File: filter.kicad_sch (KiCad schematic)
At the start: 39 parts

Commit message: Update
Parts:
- removed C12, C14, C15, C17: C,IEC, symbol PCM_Generic-50:C,IEC
- removed C13, C16: C,IEC, symbol PCM_Generic:C,IEC
- removed R16, R17, R18, R20, R21, R22: R,IEC, symbol PCM_Generic:R,IEC
- added C18, C20: C,IEC, symbol PCM_Generic-50:C,IEC
- added C19: C,IEC, symbol PCM_Generic:C,IEC
- added R23, R24: R,IEC, symbol PCM_Generic:R,IEC
- R19: value R,IEC -> R HF ,IEC; Indicator + -> (none)
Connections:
- net GROUND: now also R15.1 (+); no longer C10.1 (+), C11.1 (+), R13.1 (+)
- net at C7.1 (+), R5.1 (+): now also C10.2 (-); no longer R8.1 (+)
- net at C6.2 (-), R6.1 (+): now also C1.2 (-), R1.1 (+), R13.2 (-); no longer R8.2 (-)
- net at C5.1 (+), R11.1 (+): no longer C10.2 (-)
- net at C11.2 (-): now also C2.1 (+), R2.1 (+)
- net at R9.1 (+): now also C19.1 (+), R23.2 (-); no longer R13.2 (-)
- net at C9.2 (-), R12.1 (+): now also R8.2 (-), C19.2 (-), R24.1 (+); no longer R9.2 (-)
- net at R15.2 (-): now also R8.1 (+)
- new net: C18.1 (+), C20.2 (-), R24.2 (-)
- new net: C18.2 (-), R9.2 (-)
- new net: C10.1 (+), C11.1 (+), R7.1 (+)
- new net: R13.1 (+), R19.2 (-), R7.2 (-)
- new net: C20.1 (+), R23.1 (+)
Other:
- note added: "Update 30/04/2023"
- moved on the sheet: C1, C10, C11, C2, C3, C4, C5, C6, C7, C8, C9, R1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

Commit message: Upgrade
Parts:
- removed C10, C11, C19: C,IEC, symbol PCM_Generic:C,IEC
- removed C18, C4, C5: C,IEC, symbol PCM_Generic-50:C,IEC
- added C10, C11, C12, C13, C19, C21, C22: C,IEC, symbol PCM_Generic-50:C,IEC
- added C14, C15, C16, C17, C18, C23, C24, C4, C5: C,IEC, symbol PCM_Generic:C,IEC
- added R16, R17, R18, R20, R21, R22, R25, R26, R27, R28, R29, R30, R31, R32: R,IEC, symbol PCM_Generic:R,IEC
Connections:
- net at C2.2 (-), R1.2 (-): now also C4.1 (+); no longer C3.1 (+)
- net at R11.1 (+): now also C9.1 (+), R12.2 (-)
- net at R5.1 (+): now also C1.2 (-), C6.2 (-), C9.2 (-), R10.1 (+), R13.1 (+), R19.1 (+), R3.1 (+), C16.2 (-), C17.2 (-), C18.2 (-), R17.1 (+), R18.1 (+), R20.1 (+), R21.1 (+), R26.1 (+); no longer C7.1 (+)
- net at R24.2 (-): now also C15.2 (-), C19.2 (-); no longer C20.2 (-)
- net at R9.2 (-): now also C6.1 (+), R8.1 (+)
- net at R7.1 (+): now also C8.1 (+), R9.1 (+)
- net at C2.1 (+): now also C3.2 (-), R3.2 (-); no longer R2.1 (+)
- net at R10.2 (-): now also C7.1 (+), C8.2 (-)
- net at R15.2 (-): now also R23.2 (-), R18.2 (-), R22.2 (-), R28.2 (-); no longer R8.1 (+)
- net at R14.1 (+): now also C16.1 (+), R27.2 (-)
- net at R14.2 (-): now also C12.2 (-), C23.1 (+)
- net at R4.2 (-): now also R5.2 (-), R6.2 (-), R7.2 (-); no longer C8.2 (-)
- net at C20.1 (+), R23.1 (+): now also R25.1 (+)
- net at C1.1 (+), R2.2 (-): now also R1.1 (+); no longer R3.1 (+)
- net GROUND: no longer names the net of R15.1 (+)
- net GROUND: now also R12.1 (+), C11.1 (+)
- new net: C18.1 (+), R24.1 (+), R25.2 (-)
- new net: C23.2 (-), C24.1 (+), R32.1 (+)
- new net: C4.2 (-), C5.1 (+), R6.1 (+)
- new net: C19.1 (+), C20.2 (-), R26.2 (-)
- new net: R17.2 (-), R19.2 (-), R30.2 (-), R31.2 (-), R32.2 (-)
- new net: C12.1 (+), C21.2 (-), R20.2 (-)
- new net: C5.2 (-), C7.2 (-), R8.2 (-)
- new net: C21.1 (+), R27.1 (+), R30.1 (+)
- new net: C10.2 (-), C14.1 (+), R11.2 (-)
- new net: C14.2 (-), C15.1 (+), R22.1 (+)
- new net: C3.1 (+), R2.1 (+), R4.1 (+)
- new net: C10.1 (+), C11.2 (-), R13.2 (-)
- new net: C13.1 (+), C22.2 (-), R21.2 (-)
- new net: C22.1 (+), R29.1 (+), R31.1 (+)
- new net: C17.1 (+), R16.1 (+), R29.2 (-)
- new net: C13.2 (-), C24.2 (-), R16.2 (-)
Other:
- note removed: "LINE"
- note removed: "MC 1230"
- note removed: "NEUTRAL"
- moved on the sheet: R19

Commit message: Upgrade
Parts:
- added R33, R34: R,IEC, symbol PCM_Generic:R,IEC
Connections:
- net at C15.2 (-), C19.2 (-), R24.2 (-): now also R34.1 (+)
- net at R15.2 (-), R18.2 (-), R22.2 (-)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: now also R34.2 (-)
- net at C10.2 (-), C14.1 (+), R11.2 (-): now also R33.1 (+)
- net at C11.1 (+), R12.1 (+), R15.1 (+): now also R33.2 (-)
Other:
- note added: "12"
- note added: "In real life"
- note added: "MC 1230"
- note added: "Update 17/07/2023"
- note removed: "1"
- note removed: "Update 30/04/2023"
- moved on the sheet: R17

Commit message: Upgrade
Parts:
- removed R15, R23, R7: R,IEC, symbol PCM_Generic:R,IEC
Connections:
- net at C23.2 (-), C24.1 (+), R32.1 (+): now also R17.2 (-), R19.2 (-), R30.2 (-), R32.2 (-)
- net at C1.2 (-), C16.2 (-), C17.2 (-)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: now also R30.1 (+), R31.1 (+), R4.1 (+)
- net at R18.2 (-), R22.2 (-), R28.2 (-)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: now also R4.2 (-)
- net at C21.1 (+), R27.1 (+): no longer R30.1 (+)
- net at R5.2 (-), R6.2 (-): now also R31.2 (-); no longer R4.2 (-)
- net at C3.1 (+), R2.1 (+): no longer R4.1 (+)
- net at C22.1 (+), R29.1 (+): no longer R31.1 (+)
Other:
- moved on the sheet: R17, R30, R31, R4

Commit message: Upgrade
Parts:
- added C25, C26: C,IEC, symbol PCM_Generic:C,IEC
- added R15, R23, R35, R7: R,IEC, symbol PCM_Generic:R,IEC
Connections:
- net at C1.2 (-), C16.2 (-), C17.2 (-)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: now also R28.1 (+), C25.2 (-), C26.1 (+), R15.1 (+), R23.2 (-), R35.2 (-)
- net at R18.2 (-), R22.2 (-), R28.2 (-)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: now also C14.2 (-), C15.1 (+), R22.1 (+), R23.1 (+)
- net at C21.1 (+), R27.1 (+): now also R7.2 (-)
- net at C22.1 (+), R29.1 (+): now also R7.1 (+)
- new net: R15.2 (-), R35.1 (+)
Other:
- note added: "Updated 2023.07.22"

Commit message: Upgrade
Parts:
- removed R34, R35: R,IEC, symbol PCM_Generic:R,IEC
- added L1: L,IEC, symbol PCM_Generic:L,IEC
- added Mic1, Mic2: X-mic, symbol PCM_Elektuur:X-mic
- added R37, R38, R39, R40, R41, R42, R43, R44, R45, R46, R47, R48, R49, R50, R51, R52, R53, R54: R,IEC, symbol PCM_Generic:R,IEC
- added Re1, Re10, Re11, Re12, Re13, Re14, Re15, Re16, Re17, Re18, Re2, Re3, Re4, Re5, Re6, Re7, Re8, Re9: Re, symbol PCM_Elektuur:Re
- added U1: ${SIM.PARAMS}, symbol PCM_Generic:X-comparator,IEC
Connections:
- net PE: now also R37.2 (-), R38.2 (-), R39.2 (-), R40.2 (-), R41.2 (-), R42.2 (-), R43.2 (-), R44.2 (-), R45.2 (-), R46.2 (-), R47.2 (-), R48.2 (-), R49.2 (-), R50.2 (-), R51.2 (-), R52.2 (-), R53.2 (-), R54.2 (-)
- net at C22.1 (+), R29.1 (+): no longer R7.1 (+)
- net at C21.1 (+), R27.1 (+): no longer R7.2 (-)
- net at R17.2 (-), R19.2 (-), R30.2 (-)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: now also L1.2 (-); no longer C23.2 (-), C24.1 (+), R32.1 (+)
- net at C1.2 (-), C16.2 (-), C17.2 (-)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: no longer C18.2 (-), C9.2 (-), R13.1 (+), R18.1 (+), R26.1 (+), R4.1 (+)
- net at C10.2 (-), C14.1 (+), R11.2 (-): no longer R33.1 (+)
- net at C11.1 (+), R12.1 (+): no longer R33.2 (-)
- new net: Re1.1 (+), Re10.1 (+), Re11.1 (+), Re12.1 (+), Re13.1 (+), Re14.1 (+), Re15.1 (+), Re16.1 (+), Re17.1 (+), Re18.1 (+), Re2.1 (+), Re3.1 (+), Re4.1 (+), Re5.1 (+), Re6.1 (+), Re7.1 (+), Re8.1 (+), Re9.1 (+)
- new net: R46.1 (+), Re15.2 (-)
- new net: C23.2 (-), C24.1 (+), L1.1 (+), R32.1 (+)
- new net: Mic2.1 (+), U1.3 (V+)
- new net: C18.2 (-), C9.2 (-), R13.1 (+), R18.1 (+), R26.1 (+), R33.1 (+)
- new net: R18.2 (-), R22.2 (-), R33.2 (-)
- new net: R43.1 (+), Re4.2 (-)
- new net: R39.1 (+), Re12.2 (-)
- new net: R38.1 (+), Re11.2 (-)
- new net: C14.2 (-), C15.1 (+), R22.1 (+)
- new net: R37.1 (+), Re10.2 (-)
- new net: R49.1 (+), Re7.2 (-)
- new net: R54.1 (+), Re18.2 (-)
- new net: R45.1 (+), Re14.2 (-)
- new net: R44.1 (+), Re5.2 (-)
- new net: R48.1 (+), Re6.2 (-)
- new net: R52.1 (+), Re17.2 (-)
- new net: R50.1 (+), Re8.2 (-)
- new net: R51.1 (+), Re16.2 (-)
- new net: R23.1 (+), R28.2 (-)
- new net: R40.1 (+), Re13.2 (-)
- new net: R47.1 (+), Re1.2 (-)
- new net: R53.1 (+), Re9.2 (-)
- new net: R42.1 (+), Re3.2 (-)
- new net: R41.1 (+), Re2.2 (-)
- new net: Mic1.2 (-), U1.4 (V-)
- now unconnected: R4.2 (-)
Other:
- note added: "Must be OSHW"
- note added: "Updated 2023.08.09"
- note removed: "Updated 2023.07.22"
- moved on the sheet: C4, C5, R15, R29, R30, R31, R33, R4, R5, R6, R7

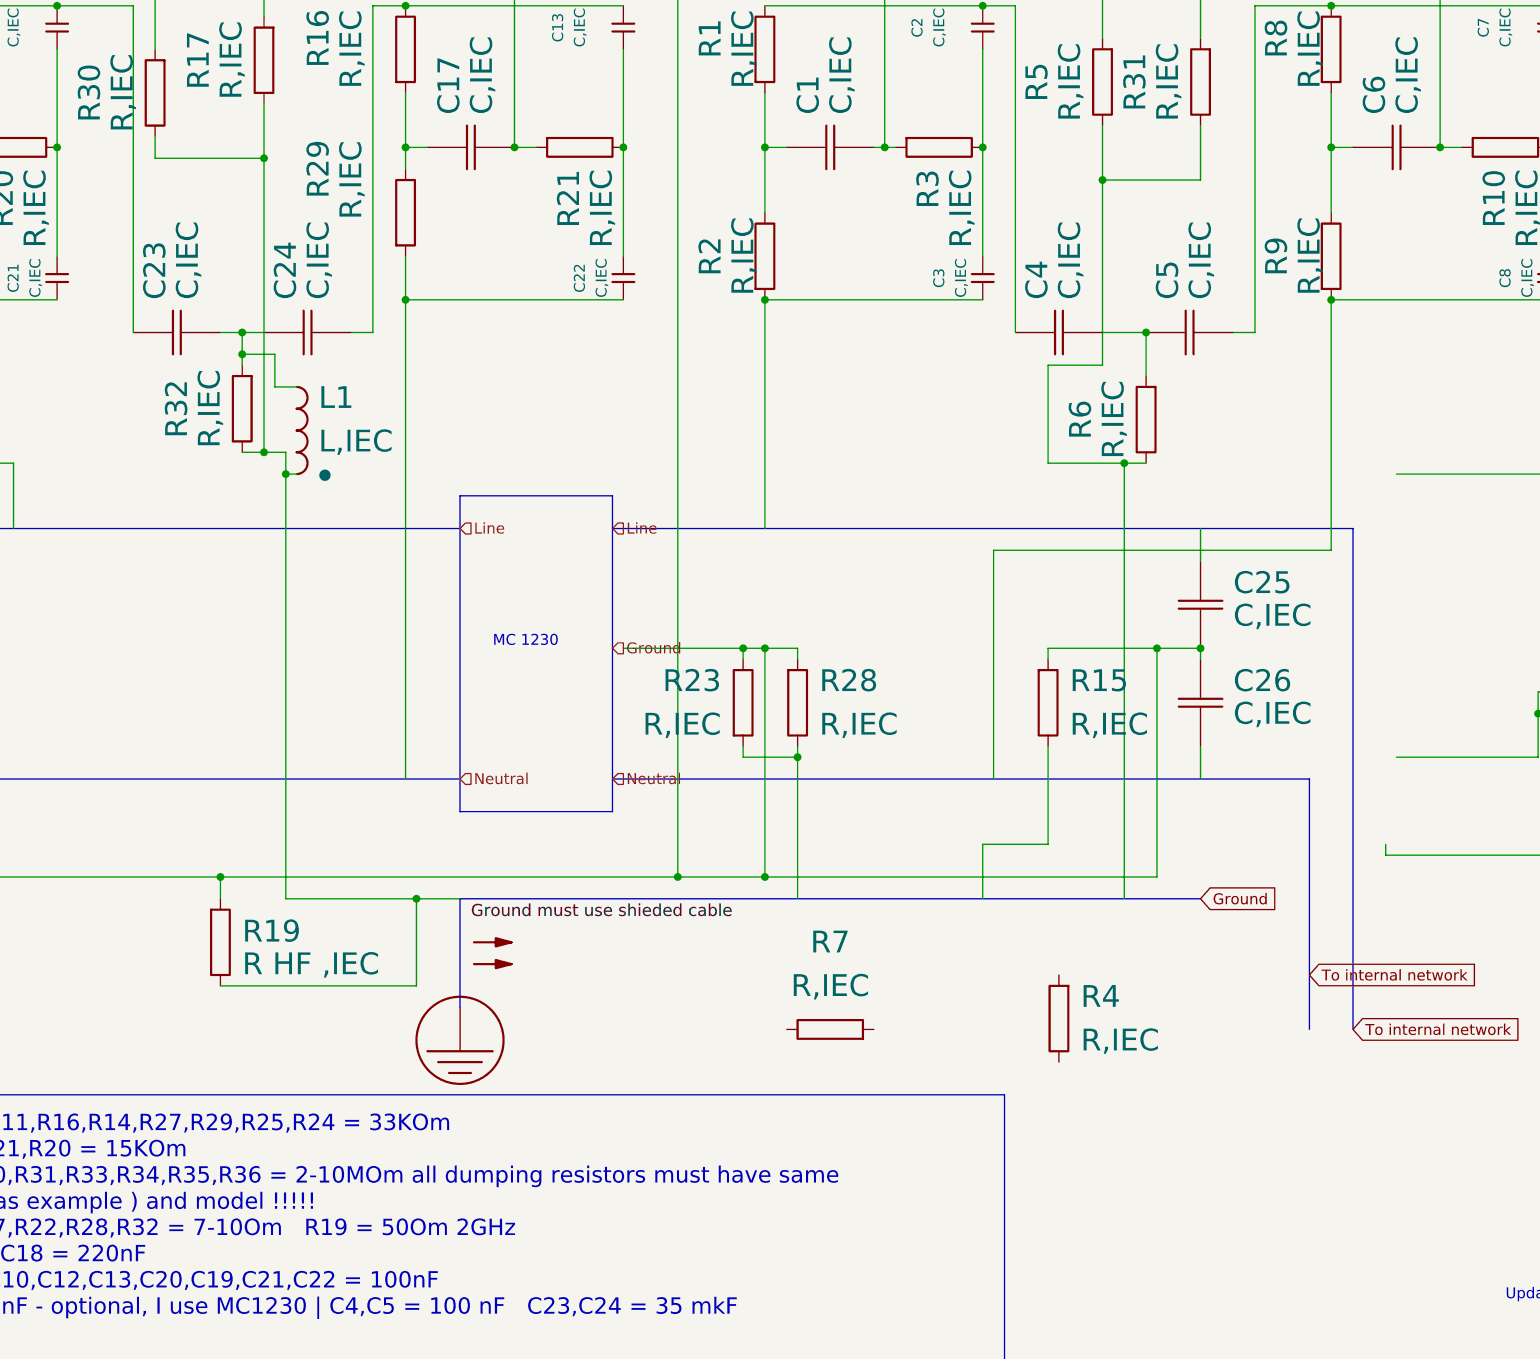
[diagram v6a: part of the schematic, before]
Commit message: Upgrader to Grounding device
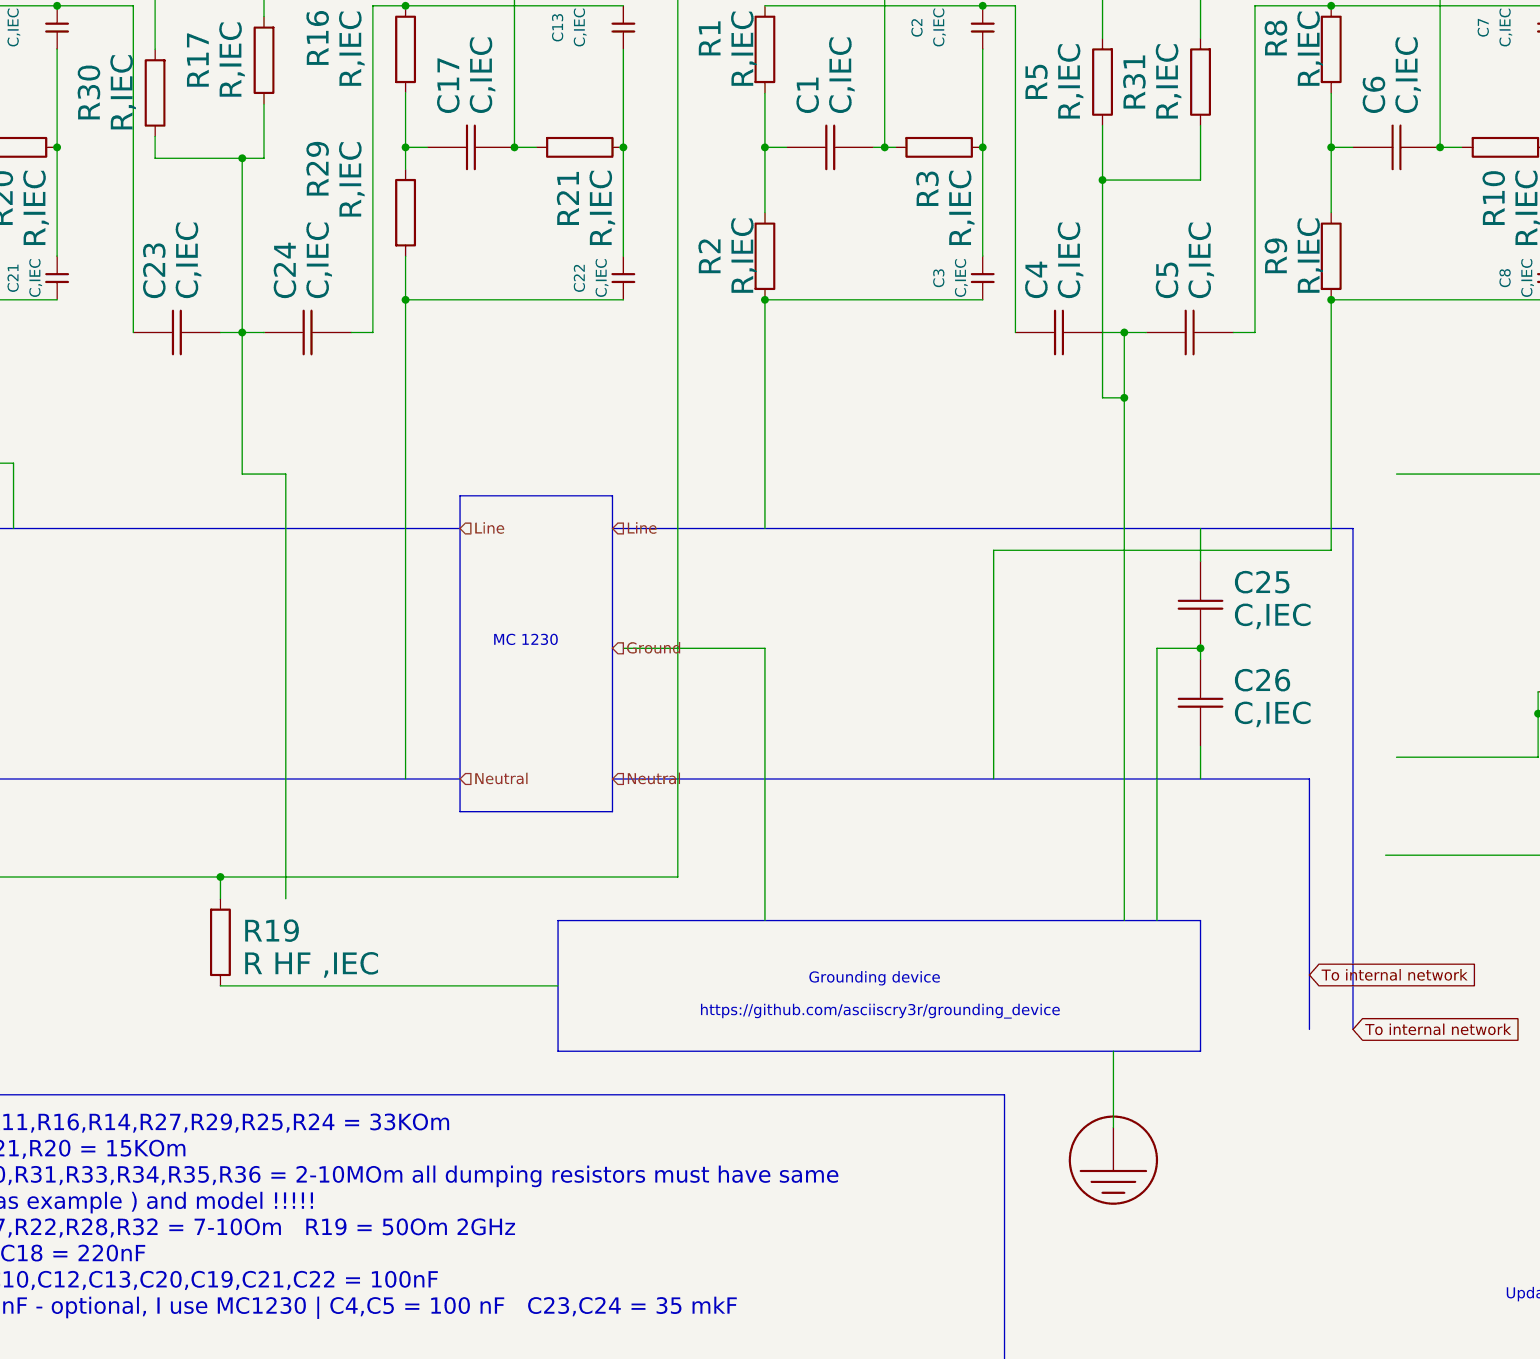
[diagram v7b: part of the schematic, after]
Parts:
- removed L1: L,IEC, symbol PCM_Generic:L,IEC
- removed R15, R23, R28, R32, R4, R6, R7: R,IEC, symbol PCM_Generic:R,IEC
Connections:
- net at C23.2 (-), C24.1 (+): now also R17.2 (-), R30.2 (-)
- net at C4.2 (-), C5.1 (+): now also R31.2 (-), R5.2 (-)
- net at C1.2 (-), C16.2 (-), C17.2 (-)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: no longer C25.2 (-), C26.1 (+)
- new net: C25.2 (-), C26.1 (+)
- now unconnected: R19.2 (-)
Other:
- note added: "Grounding device"
- note added: "https://github.com/asciiscry3r/grounding_device"
